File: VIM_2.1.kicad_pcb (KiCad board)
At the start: 2 copper layers, 83.9 x 89.5 mm, 160 parts, among them J1 BARREL_JACK, J2 Sliding switch, J3 Conn_01x05, J5 uart, J7 Conn_01x02, J8 Conn_01x03, P1 USB_OTG, P10 speed input, P12 CONN_02X03, P5 charging, P6 CONN_01X05, P9 throtle, Q1 Q_NPN_BEC, Q10 Q_NPN_BEC, Q11 Q_NPN_BEC, Q12 Q_NPN_BEC, Q13 Q_NPN_BEC, Q2 Q_NPN_BEC, Q3 Q_NPN_BEC, Q4 Q_NPN_BEC, Q5 Q_NPN_BEC, Q6 Q_NPN_BEC, Q7 Q_NPN_BEC, Q8 Q_NPN_BEC, Q9 Q_NPN_BEC, U1 STM32F405RG, U10 emmc, U11 TJA1042T/3, U12 NUP5150, U14 LD1117, U15 ufl, U16 ufl, U17 ufl, U18 ufl, U19 ublox_m8u, U2 MPU6050, U3 MIC29302, U4 ncs20062, U5 J502, U6 AP131-33, U7 MC6O, U8 lm2596 - 5v, U9 LD1117S33CTR, Y1 Crystal

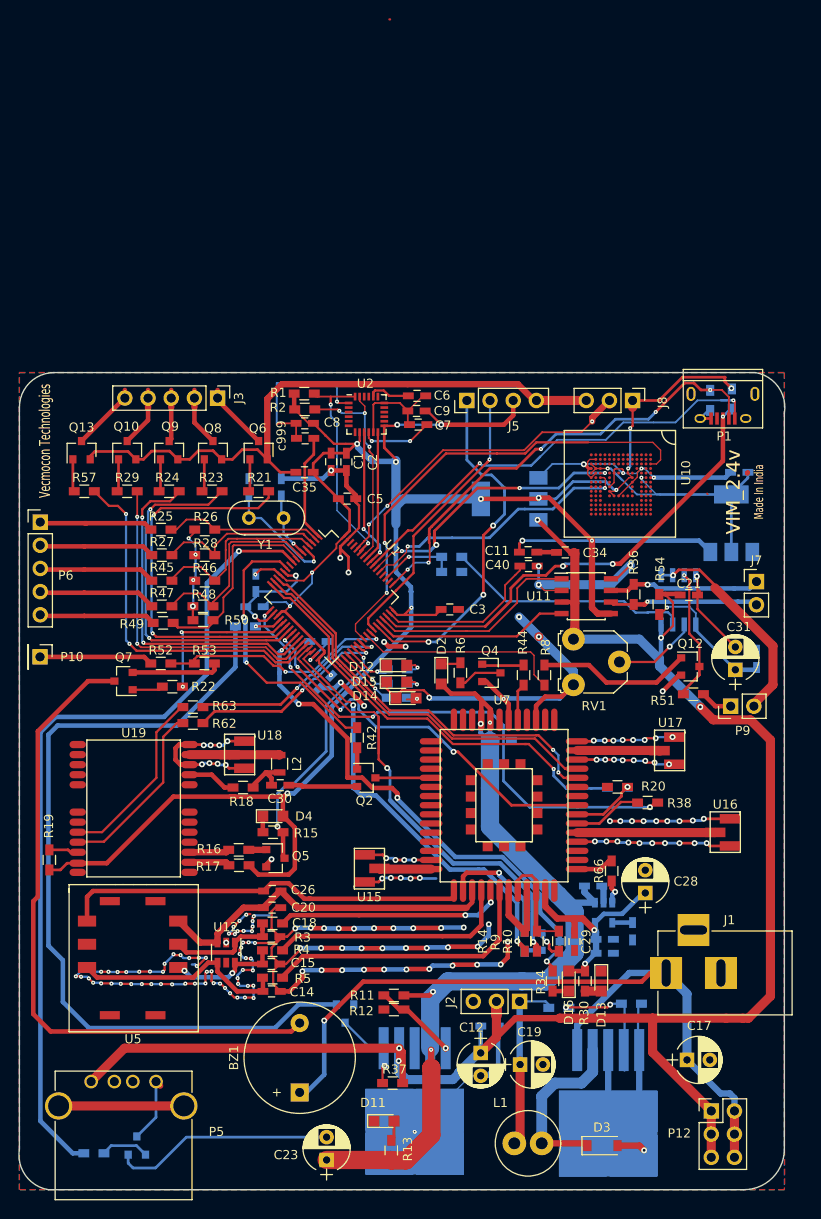
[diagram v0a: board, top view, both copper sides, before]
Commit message: Final pcb given to pcbpower
fleet management vim with following features
- ublox m8u, mc60
- mpu6050
- vibration sensor
- buzzer, switches, thottle bypass,
- sim interface according to quectel
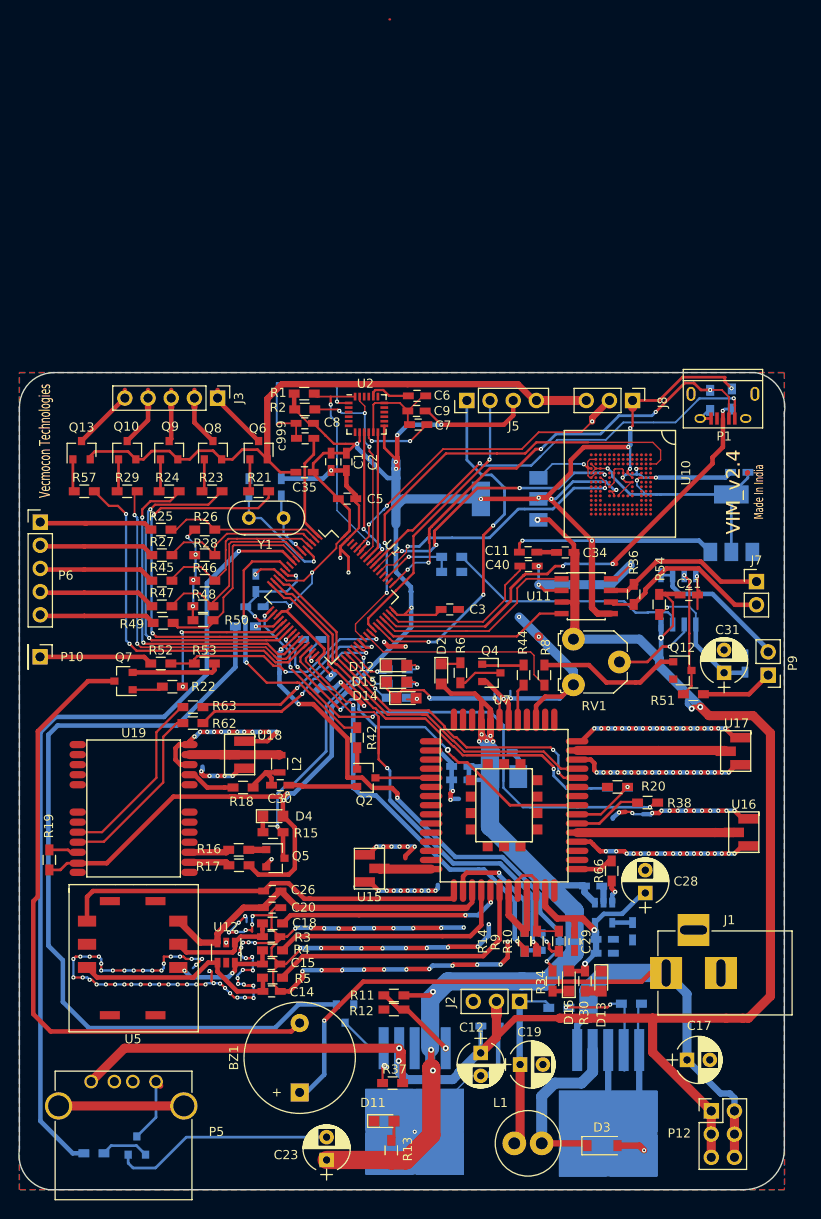
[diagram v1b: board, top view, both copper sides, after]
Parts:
- added C33: 100uF, Capacitors_Tantalum_SMD:CP_Tantalum_Case-B_EIA-3528-21_Reflow, B.Cu at (163.6, 105.9)
- added C36: 10pF, Capacitors_SMD:C_0603_HandSoldering, B.Cu at (158.8, 104.7)
- added C37: 33pF, Capacitors_SMD:C_0603_HandSoldering, B.Cu at (158.8, 106.2)
- C14, C15, C18, C20: value 10pF -> 33pF
- C23: value 100uF -> 470uF
- U10: footprint emmc1:eMMC1 -> emmc1:eMMC2.4
- U12: value NUP5150 -> CM1224
- U19: value ublox_m8u -> vim
- moved U17 7.24 mm to (189.5, 101.6)
- moved P9 5.33 mm to (192.5, 94.7), turned to 180 degrees
- moved U16 2.03 mm to (190.4, 110.5)
- moved C24 1.37 mm to (163.5, 103.2)
- moved C32 1.37 mm to (190.0, 93.5)
- moved C31 1.28 mm to (187.7, 94.5)
- moved Q12 0.97 mm to (183.1, 94.2)
- moved C10 0.71 mm to (142.6, 90.8)
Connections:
- J2 pad 3: (no net) -> Net-(J2-Pad3)
- P1 pad 4: (no net) -> Net-(P1-Pad4)
- P5 pad 2: (no net) -> Net-(P5-Pad2)
- P5 pad 3: (no net) -> Net-(P5-Pad3)
- U1 pad 10: (no net) -> Net-(U1-Pad10)
- U1 pad 50: (no net) -> Net-(U1-Pad50)
- U1 pad 52: (no net) -> Net-(U1-Pad52)
- U1 pad 61: (no net) -> Net-(U1-Pad61)
- U1 pad 62: (no net) -> Net-(U1-Pad62)
- U10 pad 10: (no net) -> Net-(U10-Pad10)
- U10 pad 100: (no net) -> Net-(U10-Pad100)
- U10 pad 101: (no net) -> Net-(U10-Pad101)
- U10 pad 102: (no net) -> Net-(U10-Pad102)
- U10 pad 103: (no net) -> Net-(U10-Pad103)
- U10 pad 104: (no net) -> Net-(U10-Pad104)
- U10 pad 106: (no net) -> Net-(U10-Pad106)
- U10 pad 107: (no net) -> Net-(U10-Pad107)
- U10 pad 108: (no net) -> Net-(U10-Pad108)
- U10 pad 109: (no net) -> Net-(U10-Pad109)
- U10 pad 11: (no net) -> Net-(U10-Pad11)
- U10 pad 110: (no net) -> Net-(U10-Pad110)
- U10 pad 111: (no net) -> Net-(U10-Pad111)
- U10 pad 112: (no net) -> Net-(U10-Pad112)
- U10 pad 113: (no net) -> Net-(U10-Pad113)
- U10 pad 114: (no net) -> Net-(U10-Pad114)
- U10 pad 115: (no net) -> Net-(U10-Pad115)
- U10 pad 116: (no net) -> Net-(U10-Pad116)
- U10 pad 117: (no net) -> Net-(U10-Pad117)
- U10 pad 118: (no net) -> Net-(U10-Pad118)
- U10 pad 119: (no net) -> Net-(U10-Pad119)
- U10 pad 12: (no net) -> Net-(U10-Pad12)
- U10 pad 120: (no net) -> Net-(U10-Pad120)
- U10 pad 121: (no net) -> Net-(U10-Pad121)
- U10 pad 122: (no net) -> Net-(U10-Pad122)
- U10 pad 123: (no net) -> Net-(U10-Pad123)
- U10 pad 124: (no net) -> Net-(U10-Pad124)
- U10 pad 125: (no net) -> Net-(U10-Pad125)
- U10 pad 126: (no net) -> Net-(U10-Pad126)
- U10 pad 127: (no net) -> Net-(U10-Pad127)
- U10 pad 128: (no net) -> Net-(U10-Pad128)
- U10 pad 129: (no net) -> Net-(U10-Pad129)
- U10 pad 13: (no net) -> Net-(U10-Pad13)
- U10 pad 130: (no net) -> Net-(U10-Pad130)
- U10 pad 131: (no net) -> Net-(U10-Pad131)
- U10 pad 132: (no net) -> Net-(U10-Pad132)
- U10 pad 133: (no net) -> Net-(U10-Pad133)
- U10 pad 134: (no net) -> Net-(U10-Pad134)
- U10 pad 135: (no net) -> Net-(U10-Pad135)
- U10 pad 136: (no net) -> Net-(U10-Pad136)
- U10 pad 137: (no net) -> Net-(U10-Pad137)
- U10 pad 138: (no net) -> Net-(U10-Pad138)
- U10 pad 139: (no net) -> Net-(U10-Pad139)
- U10 pad 14: (no net) -> Net-(U10-Pad14)
- U10 pad 140: (no net) -> Net-(U10-Pad140)
- U10 pad 141: (no net) -> Net-(U10-Pad141)
- U10 pad 142: (no net) -> Net-(U10-Pad142)
- U10 pad 143: (no net) -> Net-(U10-Pad143)
- U10 pad 144: (no net) -> Net-(U10-Pad144)
- U10 pad 145: (no net) -> Net-(U10-Pad145)
- U10 pad 146: (no net) -> Net-(U10-Pad146)
- U10 pad 147: (no net) -> Net-(U10-Pad147)
- U10 pad 148: (no net) -> Net-(U10-Pad148)
- U10 pad 149: (no net) -> Net-(U10-Pad149)
- U10 pad 15: (no net) -> Net-(U10-Pad15)
- U10 pad 150: (no net) -> Net-(U10-Pad150)
- U10 pad 151: (no net) -> Net-(U10-Pad151)
- U10 pad 152: (no net) -> Net-(U10-Pad152)
- U10 pad 153: (no net) -> Net-(U10-Pad153)
- U10 pad 16: (no net) -> Net-(U10-Pad16)
- U10 pad 17: (no net) -> Net-(U10-Pad17)
- U10 pad 18: (no net) -> Net-(U10-Pad18)
- U10 pad 19: (no net) -> Net-(U10-Pad19)
- U10 pad 2: (no net) -> Net-(U10-Pad2)
- U10 pad 20: (no net) -> Net-(U10-Pad20)
- U10 pad 3: (no net) -> Net-(U10-Pad3)
- U10 pad 4: (no net) -> Net-(U10-Pad4)
- U10 pad 41: (no net) -> Net-(U10-Pad41)
- U10 pad 42: (no net) -> Net-(U10-Pad42)
- U10 pad 43: (no net) -> Net-(U10-Pad43)
- U10 pad 44: (no net) -> Net-(U10-Pad44)
- U10 pad 45: (no net) -> Net-(U10-Pad45)
- U10 pad 46: (no net) -> Net-(U10-Pad46)
- U10 pad 47: (no net) -> Net-(U10-Pad47)
- U10 pad 48: (no net) -> Net-(U10-Pad48)
- U10 pad 5: (no net) -> Net-(U10-Pad5)
- U10 pad 51: (no net) -> Net-(U10-Pad51)
- U10 pad 52: (no net) -> Net-(U10-Pad52)
- U10 pad 53: (no net) -> Net-(U10-Pad53)
- U10 pad 54: (no net) -> Net-(U10-Pad54)
- U10 pad 55: (no net) -> Net-(U10-Pad55)
- U10 pad 56: (no net) -> Net-(U10-Pad56)
- U10 pad 57: (no net) -> Net-(U10-Pad57)
- U10 pad 58: (no net) -> Net-(U10-Pad58)
- U10 pad 59: (no net) -> Net-(U10-Pad59)
- U10 pad 6: (no net) -> Net-(U10-Pad6)
- U10 pad 60: (no net) -> Net-(U10-Pad60)
- U10 pad 61: (no net) -> Net-(U10-Pad61)
- U10 pad 62: (no net) -> Net-(U10-Pad62)
- U10 pad 63: (no net) -> Net-(U10-Pad63)
- U10 pad 64: (no net) -> Net-(U10-Pad64)
- U10 pad 65: (no net) -> Net-(U10-Pad65)
- U10 pad 66: (no net) -> Net-(U10-Pad66)
- U10 pad 67: (no net) -> Net-(U10-Pad67)
- U10 pad 68: (no net) -> Net-(U10-Pad68)
- U10 pad 69: (no net) -> Net-(U10-Pad69)
- U10 pad 7: (no net) -> Net-(U10-Pad7)
- U10 pad 70: (no net) -> Net-(U10-Pad70)
- U10 pad 71: (no net) -> Net-(U10-Pad71)
- U10 pad 72: (no net) -> Net-(U10-Pad72)
- U10 pad 73: (no net) -> Net-(U10-Pad73)
- U10 pad 74: (no net) -> Net-(U10-Pad74)
- U10 pad 75: (no net) -> Net-(U10-Pad75)
- U10 pad 76: (no net) -> Net-(U10-Pad76)
- U10 pad 78: (no net) -> Net-(U10-Pad78)
- U10 pad 79: (no net) -> Net-(U10-Pad79)
- U10 pad 8: (no net) -> Net-(U10-Pad8)
- U10 pad 80: (no net) -> Net-(U10-Pad80)
- U10 pad 81: (no net) -> Net-(U10-Pad81)
- U10 pad 82: (no net) -> Net-(U10-Pad82)
- U10 pad 83: (no net) -> Net-(U10-Pad83)
- U10 pad 84: (no net) -> Net-(U10-Pad84)
- U10 pad 85: (no net) -> Net-(U10-Pad85)
- U10 pad 86: (no net) -> Net-(U10-Pad86)
- U10 pad 87: (no net) -> Net-(U10-Pad87)
- U10 pad 88: (no net) -> Net-(U10-Pad88)
- U10 pad 89: (no net) -> Net-(U10-Pad89)
- U10 pad 9: (no net) -> Net-(U10-Pad9)
- U10 pad 90: (no net) -> Net-(U10-Pad90)
- U10 pad 91: (no net) -> Net-(U10-Pad91)
- U10 pad 92: (no net) -> Net-(U10-Pad92)
- U10 pad 93: (no net) -> Net-(U10-Pad93)
- U10 pad 94: (no net) -> Net-(U10-Pad94)
- U10 pad 95: (no net) -> Net-(U10-Pad95)
- U10 pad 96: (no net) -> Net-(U10-Pad96)
- U10 pad 97: (no net) -> Net-(U10-Pad97)
- U10 pad 98: (no net) -> Net-(U10-Pad98)
- U10 pad 99: (no net) -> Net-(U10-Pad99)
- U12 pad 5: (no net) -> Net-(U12-Pad5)
- U19 pad 1: (no net) -> Net-(U19-Pad1)
- U19 pad 14: (no net) -> Net-(U19-Pad14)
- U19 pad 15: (no net) -> Net-(U19-Pad15)
- U19 pad 16: (no net) -> Net-(U19-Pad16)
- U19 pad 17: (no net) -> Net-(U19-Pad17)
- U19 pad 18: (no net) -> Net-(U19-Pad18)
- U19 pad 19: (no net) -> Net-(U19-Pad19)
- U19 pad 4: (no net) -> Net-(U19-Pad4)
- U19 pad 5: (no net) -> Net-(U19-Pad5)
- U19 pad 6: (no net) -> Net-(U19-Pad6)
- U19 pad 7: (no net) -> Net-(U19-Pad7)
- U19 pad 8: (no net) -> Net-(U19-Pad8)
- U2 pad 14: (no net) -> Net-(U2-Pad14)
- U2 pad 15: (no net) -> Net-(U2-Pad15)
- U2 pad 16: (no net) -> Net-(U2-Pad16)
- U2 pad 17: (no net) -> Net-(U2-Pad17)
- U2 pad 19: (no net) -> Net-(U2-Pad19)
- U2 pad 2: (no net) -> Net-(U2-Pad2)
- U2 pad 21: (no net) -> Net-(U2-Pad21)
- U2 pad 22: (no net) -> Net-(U2-Pad22)
- U2 pad 3: (no net) -> Net-(U2-Pad3)
- U2 pad 4: (no net) -> Net-(U2-Pad4)
- U2 pad 5: (no net) -> Net-(U2-Pad5)
- U2 pad 6: (no net) -> Net-(U2-Pad6)
- U2 pad 7: (no net) -> Net-(U2-Pad7)
- U5 pad 2: (no net) -> Net-(U5-Pad2)
- U7 pad 1: (no net) -> Net-(U7-Pad1)
- U7 pad 10: (no net) -> Net-(U7-Pad10)
- U7 pad 11: (no net) -> Net-(U7-Pad11)
- U7 pad 12: (no net) -> Net-(U7-Pad12)
- U7 pad 13: (no net) -> Net-(U7-Pad13)
- U7 pad 2: (no net) -> Net-(U7-Pad2)
- U7 pad 29: (no net) -> Net-(U7-Pad29)
- U7 pad 3: (no net) -> Net-(U7-Pad3)
- U7 pad 30: (no net) -> Net-(U7-Pad30)
- U7 pad 36: (no net) -> Net-(U7-Pad36)
- U7 pad 37: (no net) -> Net-(U7-Pad37)
- U7 pad 4: (no net) -> Net-(U7-Pad4)
- U7 pad 43: (no net) -> /MC60/VDD_EXT
- U7 pad 46: (no net) -> Net-(U7-Pad46)
- U7 pad 52: (no net) -> Net-(U7-Pad52)
- U7 pad 53: (no net) -> Net-(U7-Pad53)
- U7 pad 54: (no net) -> Net-(U7-Pad54)
- U7 pad 55: (no net) -> Net-(U7-Pad55)
- U7 pad 56: (no net) -> Net-(U7-Pad56)
- U7 pad 57: (no net) -> Net-(U7-Pad57)
- U7 pad 58: (no net) -> Net-(U7-Pad58)
- U7 pad 59: (no net) -> Net-(U7-Pad59)
- U7 pad 6: (no net) -> Net-(U7-Pad6)
- U7 pad 60: (no net) -> Net-(U7-Pad60)
- U7 pad 61: (no net) -> Net-(U7-Pad61)
- U7 pad 62: (no net) -> Net-(U7-Pad62)
- U7 pad 63: (no net) -> Net-(U7-Pad63)
- U7 pad 64: (no net) -> Net-(U7-Pad64)
- U7 pad 65: (no net) -> Net-(U7-Pad65)
- U7 pad 66: (no net) -> Net-(U7-Pad66)
- U7 pad 67: (no net) -> Net-(U7-Pad67)
- U7 pad 68: (no net) -> Net-(U7-Pad68)
- U7 pad 7: (no net) -> Net-(U7-Pad7)
- U7 pad 8: (no net) -> Net-(U7-Pad8)
- U7 pad 9: (no net) -> Net-(U7-Pad9)
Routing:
- net GND: track 596.4 -> 646.7 mm, vias 164 -> 229
- net /MC60/vbat: track 127.8 -> 149.7 mm, vias 4 -> 8
- net +3V3: track 284.1 -> 299.4 mm, vias 18 -> 22
- net (no net): track 12.7 -> 2.79 mm, vias 13 -> 2
- net Net-(P9-Pad2): track 23.6 -> 16.1 mm, vias 1 -> 0
- net Net-(U17-Pad1): track 9.08 -> 16.3 mm
- net Net-(P9-Pad1): track 3.75 -> 7.96 mm
- net Net-(J7-Pad2): track 17.2 -> 20.9 mm, vias 1 -> 0
- net +5V: track 209.2 -> 212.2 mm, vias 5 -> 6
- net Net-(P1-Pad3): track 60.8 -> 58.2 mm
- net Net-(U16-Pad1): track 15.2 -> 17.2 mm
- net +12V: track 88.0 -> 89.6 mm
- net Net-(J7-Pad1): track 17.0 -> 18.5 mm, vias 1 -> 0
- net /ublox/gnss_rx: track 23.7 -> 22.5 mm
- net Net-(Q12-Pad1): track 17.0 -> 15.8 mm
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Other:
- net class Default: clearance 0.1 -> 0.125; via_dia 0.65 -> 0.46; via_drill 0.3 -> 0.17
- net class vbat added: clearance 0.125, trace_width 0.25, via_dia 0.65, via_drill 0.17
- net class vim: clearance 0.1 -> 0.125; via_drill 0.3 -> 0.35
- net class vim2 added: clearance 0.125, trace_width 0.25, via_dia 0.46, via_drill 0.2
- rule trace_clearance: 0.1 -> 0.125
- rule trace_min: 0.15 -> 0.125
- rule via_min_drill: 0.15 -> 0.17
- rule via_min_size: 0.45 -> 0.46
- board text added: "VIM_v2.4"
- board text removed: "VIM_2.4v"

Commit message: pcb print 28 jul
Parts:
- removed P10: speed input, Pin_Headers:Pin_Header_Straight_1x01_Pitch2.54mm
- removed P5: charging, Connectors:USB_A
- removed P6: CONN_01X05, Pin_Headers:Pin_Header_Straight_1x05_Pitch2.54mm
- removed U16: ufl, ufl:ufl_shield
- added AE1: Antenna, chip antenna:chip antenaa, F.Cu at (189.2, 112.0)
- added C41: 100nf, Capacitors_SMD:C_0603_HandSoldering, F.Cu at (149.9, 92.1)
- added D1: D, Diodes_SMD:D_SOD-123, B.Cu at (128.0, 138.2)
- added G***: LOGO, logo:logo3, F.Cu at (114.5, 140.4)
- added G***: LOGO, logo:logo5, B.Cu at (117.7, 141.4)
- added J4: Conn_01x06, Pin_Headers:Pin_Header_Straight_1x06_Pitch2.54mm, F.Cu at (114.6, 78.1)
- added P2: charging, Pin_Headers:Pin_Header_Straight_1x02_Pitch2.54mm, F.Cu at (141.9, 147.7)
- C12, C19: footprint Capacitors_THT:CP_Radial_D5.0mm_P2.50mm -> Capacitors_SMD:CP_Elec_6.3x5.7
- C17: footprint Capacitors_THT:CP_Radial_D5.0mm_P2.50mm -> Capacitors_SMD:CP_Elec_8x6.7
- C23: footprint Capacitors_THT:CP_Radial_D5.0mm_P2.50mm -> Capacitors_SMD:CP_Elec_8x10
- C28: footprint Capacitors_THT:CP_Radial_D5.0mm_P2.50mm -> Capacitors_SMD:CP_Elec_5x5.3
- C33: footprint Capacitors_Tantalum_SMD:CP_Tantalum_Case-B_EIA-3528-21_Reflow -> Capacitors_Tantalum_SMD:CP_Tantalum_Case-D_EIA-7343-31_Reflow
- L1: footprint Inductors_THT:L_Radial_D7.0mm_P3.00mm -> Inductors_SMD:L_7.3x7.3_H3.5
- moved Q11 12.0 mm to (135.2, 147.9), turned to 0 degrees
- moved C12 11.9 mm to (149.3, 138.2), turned to 180 degrees
- moved R13 10.3 mm to (141.8, 142.6), turned to 180 degrees
- moved C23 9.85 mm to (153.9, 146.3), turned to 180 degrees
- moved BZ1 9.48 mm to (131.8, 141.5), turned to 180 degrees
- moved D11 9.11 mm to (141.7, 141.1), turned to 180 degrees
- moved C17 7.65 mm to (176.1, 138.2)
- moved R7 6.89 mm to (125.3, 149.0)
- moved R37 6.74 mm to (151.3, 132.7)
- moved C32 6.10 mm to (186.6, 88.4)
- moved C33 5.41 mm to (164.3, 100.5)
- moved P12 3.22 mm to (185.0, 139.6), turned to 90 degrees
- moved C22 2.49 mm to (186.9, 72.3)
- moved Q12 2.03 mm to (181.1, 94.2)
- moved C28 1.87 mm to (180.7, 117.7), turned to 0 degrees
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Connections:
- R52 pad 1: Net-(P10-Pad1) -> /STM32 mcu/hall
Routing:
- net +12V: track 89.6 -> 113.5 mm, vias 1 -> 4
- net GND: track 646.7 -> 625.0 mm, vias 229 -> 230
- net +5V: track 212.2 -> 195.7 mm
- net Net-(P5-Pad5): track 13.7 -> 0.00 mm
- net Net-(P10-Pad1): track 12.4 -> 0.00 mm
- net /STM32 mcu/hall: track 0.00 -> 12.0 mm
- net /MC60/vbat: track 149.7 -> 139.6 mm
- net Net-(BZ1-Pad2): track 72.2 -> 62.2 mm
- net Net-(C19-Pad1): track 21.0 -> 27.4 mm, vias 0 -> 2
- net Net-(Q1-Pad3): track 9.33 -> 15.6 mm
- net Net-(D3-Pad1): track 19.4 -> 25.5 mm, vias 0 -> 3
- net Net-(J3-Pad5): track 7.85 -> 13.5 mm
- net Net-(R64-Pad1): track 14.3 -> 19.4 mm
- net Net-(J3-Pad1): track 8.17 -> 13.3 mm
- net /STM32 mcu/charging: track 91.1 -> 94.9 mm
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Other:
- outline, holes or cut-outs redrawn

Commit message: bt
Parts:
- AE1: footprint chip antenna:chip antenaa -> ANTENNASMD:bluetooth_antenna
- moved AE1 0.33 mm to (188.8, 111.9)
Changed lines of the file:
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@@
   (general
     (links 397)
-    (no_connects 0)
-    (area 110.362445 61.519999 194.437555 151.205001)
+    (no_connects 67)
+    (area 109.932181 22.646319 206.605 157.560001)
     (thickness 1.6)
     (drawings 18)
@@
   )
   (setup
-    (last_trace_width 0.5)
+    (last_trace_width 0.25)
     (user_trace_width 0.125)
     (user_trace_width 0.2)
@@
     )
   )
-  (module "chip antenna:chip antenaa" (layer F.Cu)
-    (at 189.1538 111.9759)
-    (fp_text reference AE1 (at 1.0668 -1.778) (layer F.SilkS)
-      (effects (font (size 1 1) (thickness 0.15)))
-    )
-    (fp_text value Antenna (at 1.1684 1.4224) (layer F.Fab)
-      (effects (font (size 1 1) (thickness 0.15)))
-    )
-    (fp_arc (start 0.6604 0) (end 1.0668 -0.4064) (angle 90) (layer F.SilkS) (width 0.15))
-    (fp_line (start -0.762 -0.9144) (end 3.7084 -0.9144) (layer F.SilkS) (width 0.15))
-    (fp_line (start 3.7084 -0.9144) (end 3.7592 -0.9144) (layer F.SilkS) (width 0.15))
-    (fp_line (start 3.7592 -0.9144) (end 3.7592 0.9144) (layer F.SilkS) (width 0.15))
-    (fp_line (start 3.7592 0.9144) (end -0.8128 0.9144) (layer F.SilkS) (width 0.15))
-    (fp_line (start -0.8128 0.9144) (end -0.8128 -0.9144) (layer F.SilkS) (width 0.15))
-    (pad 1 smd rect (at 0 0) (size 1.5 1.8) (layers F.Cu F.Paste F.Mask)
-      (net 327 "Net-(AE1-Pad1)"))
-    (pad "" smd rect (at 3 0) (size 1.5 1.8) (layers F.Cu F.Paste F.Mask))
-  )
   (module Capacitors_Tantalum_SMD:CP_Tantalum_Case-D_EIA-7343-31_Reflow (layer B.Cu)
     (at 164.2618 100.4951)
@@
       (xy -4.097867 0.143934)) (layer B.SilkS) (width 0.01))
   )
+  (module ANTENNASMD:bluetooth_antenna (layer F.Cu)
+    (at 188.8236 111.9251)
+    (fp_text reference AE1 (at 3.175 2.54) (layer F.SilkS)
+      (effects (font (size 1 1) (thickness 0.15)))
+    )
+    (fp_text value Antenna (at 2.54 -2.54) (layer F.Fab)
+      (effects (font (size 1 1) (thickness 0.15)))
+    )
+    (pad 1 smd rect (at 0 0) (size 0.8 2) (layers F.Cu F.Paste F.Mask)
+      (net 327 "Net-(AE1-Pad1)"))
+    (pad "" smd rect (at 4.7 0) (size 0.8 2) (layers F.Cu F.Paste F.Mask))
+    (pad "" smd rect (at 2.35 -0.85) (size 2.8 0.7) (layers F.Cu F.Paste F.Mask))
+    (pad "" smd rect (at 2.35 0.85) (size 2.8 0.7) (layers F.Cu F.Paste F.Mask))
+  )
   (gr_circle (center 114.1222 65.0367) (end 116.0272 65.0367) (layer Edge.Cuts) (width 0.15))
   (gr_circle (center 191.1858 70.9803) (end 193.0908 70.9803) (layer Edge.Cuts) (width 0.15))
@@
   (segment (start 117.2718 92.75) (end 124.162 92.75) (width 0.5) (layer F.Cu) (net 333))
   (segment (start 124.162 92.75) (end 124.884 93.472) (width 0.5) (layer F.Cu) (net 333))
-  (zone (net 2) (net_name GND) (layer B.Cu) (hatch edge 0.508)
+  (zone (net 0) (net_name "") (layer B.Cu) (hatch edge 0.508)
     (connect_pads (clearance 0.508))
     (min_thickness 0.254)
-    (fill yes (arc_segments 16) (thermal_gap 0.508) (thermal_bridge_width 0.508))
+    (keepout (tracks allowed) (vias allowed) (copperpour not_allowed))
+    (fill (arc_segments 16) (thermal_gap 0.508) (thermal_bridge_width 0.508))
     (polygon
       (pts
-        (xy 194.31 151.13) (xy 110.49 151.13) (xy 110.49 61.595) (xy 194.31 61.595)
+        (xy 194.5132 118.6053) (xy 188.1632 118.6053) (xy 188.1632 105.9053) (xy 194.5132 105.9053)
       )
     )
   )
-  (zone (net 2) (net_name GND) (layer F.Cu) (hatch edge 0.508)
-    (connect_pads (clearance 0.16))
+  (zone (net 0) (net_name "") (layer F.Cu) (hatch edge 0.508)
+    (connect_pads (clearance 0.508))
     (min_thickness 0.254)
-    (fill yes (arc_segments 16) (thermal_gap 0.508) (thermal_bridge_width 0.508))
+    (keepout (tracks allowed) (vias allowed) (copperpour not_allowed))
+    (fill (arc_segments 16) (thermal_gap 0.508) (thermal_bridge_width 0.508))
     (polygon
       (pts
-        (xy 194.31 140.410252) (xy 194.34 150.906) (xy 194.31 150.906) (xy 194.31 151.13) (xy 110.49 151.13)
-        (xy 110.49 61.595) (xy 194.31 61.595)
+        (xy 194.5132 118.6053) (xy 188.1632 118.6053) (xy 188.1632 105.9053) (xy 194.5132 105.9053)
       )
     )
   )
-  (zone (net 0) (net_name "") (layer B.Cu) (hatch edge 0.508)
+  (zone (net 2) (net_name GND) (layer B.Cu) (hatch edge 0.508)
     (connect_pads (clearance 0.508))
     (min_thickness 0.254)
-    (keepout (tracks allowed) (vias allowed) (copperpour not_allowed))
     (fill (arc_segments 16) (thermal_gap 0.508) (thermal_bridge_width 0.508))
     (polygon
       (pts
-        (xy 194.5132 118.6053) (xy 188.1632 118.6053) (xy 188.1632 105.9053) (xy 194.5132 105.9053)
+        (xy 194.31 151.13) (xy 110.49 151.13) (xy 110.49 61.595) (xy 194.31 61.595)
       )
     )
   )
-  (zone (net 0) (net_name "") (layer F.Cu) (hatch edge 0.508)
-    (connect_pads (clearance 0.508))
+  (zone (net 2) (net_name GND) (layer F.Cu) (hatch edge 0.508)
+    (connect_pads (clearance 0.16))
     (min_thickness 0.254)
-    (keepout (tracks allowed) (vias allowed) (copperpour not_allowed))
     (fill (arc_segments 16) (thermal_gap 0.508) (thermal_bridge_width 0.508))
     (polygon
       (pts
-        (xy 194.5132 118.6053) (xy 188.1632 118.6053) (xy 188.1632 105.9053) (xy 194.5132 105.9053)
+        (xy 194.31 140.410252) (xy 194.34 150.906) (xy 194.31 150.906) (xy 194.31 151.13) (xy 110.49 151.13)
+        (xy 110.49 61.595) (xy 194.31 61.595)
       )
     )

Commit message: final
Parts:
- removed P12: CONN_02X03, Pin_Headers:Pin_Header_Straight_2x03_Pitch2.54mm
- removed P9: throtle, Pin_Headers:Pin_Header_Straight_1x02_Pitch2.54mm
- added J10: Conn_01x03, Pin_Headers:Pin_Header_Straight_1x03_Pitch2.54mm, F.Cu at (114.9, 91.8)
- added J6: Conn_01x03, Pin_Headers:Pin_Header_Straight_1x03_Pitch2.54mm, F.Cu at (185.7, 136.1)
- added J9: Conn_01x03, Pin_Headers:Pin_Header_Straight_1x03_Pitch2.54mm, F.Cu at (114.6, 78.1)
- J4: value Conn_01x06 -> Conn_01x03; footprint Pin_Headers:Pin_Header_Straight_1x06_Pitch2.54mm -> Pin_Headers:Pin_Header_Straight_1x03_Pitch2.54mm
- J7: value Conn_01x02 -> uart; footprint Pin_Headers:Pin_Header_Straight_1x02_Pitch2.54mm -> Pin_Headers:Pin_Header_Straight_1x04_Pitch2.54mm
- moved J4 95.7 mm to (185.5, 142.3), turned to 90 degrees
- moved Q12 4.09 mm to (179.9, 98.2)
- moved C31 3.97 mm to (181.9, 94.6)
- moved G*** 1.41 mm to (118.9, 142.1)
- moved J7 1.05 mm to (189.6, 85.7)
- moved R51 0.57 mm to (184.2, 97.4)
- moved G*** 0.24 mm to (114.6, 140.6)
- moved AE1 0.06 mm to (188.8, 111.9)
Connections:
- J4 pad 1: Net-(J4-Pad1) -> +5V
- J4 pad 2: Net-(J4-Pad2) -> +5V
- J4 pad 3: Net-(J4-Pad3) -> +5V
- R25 pad 1: Net-(J4-Pad1) -> Net-(J9-Pad1)
- R27 pad 1: Net-(J4-Pad2) -> Net-(J9-Pad2)
- R45 pad 1: Net-(J4-Pad3) -> Net-(J9-Pad3)
- R47 pad 1: Net-(J4-Pad4) -> Net-(J10-Pad1)
- R49 pad 1: Net-(J4-Pad5) -> Net-(J10-Pad2)
- R51 pad 2: Net-(P9-Pad1) -> /STM32 mcu/a
- U4 pad 1: Net-(P9-Pad2) -> /STM32 mcu/b
- U4 pad 2: Net-(P9-Pad2) -> /STM32 mcu/b
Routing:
- net Net-(J9-Pad3): track 0.00 -> 22.9 mm
- net Net-(J9-Pad2): track 0.00 -> 21.0 mm
- net Net-(P9-Pad2): track 14.8 -> 0.00 mm, vias 1 -> 0
- net /STM32 mcu/b: track 0.00 -> 13.0 mm, vias 0 -> 1
- net Net-(J10-Pad2): track 0.00 -> 12.5 mm
- net Net-(J4-Pad3): track 12.0 -> 0.00 mm
- net Net-(J10-Pad1): track 0.00 -> 12.0 mm
- net Net-(J4-Pad5): track 11.6 -> 0.00 mm
- net Net-(J4-Pad1): track 11.6 -> 0.00 mm
- net Net-(J4-Pad2): track 11.6 -> 0.00 mm
- net Net-(J4-Pad4): track 11.5 -> 0.00 mm
- net Net-(J9-Pad1): track 0.00 -> 10.7 mm
- net +12V: track 113.5 -> 120.5 mm
- net Net-(P9-Pad1): track 6.58 -> 0.00 mm
- net /STM32 mcu/a: track 0.00 -> 5.92 mm
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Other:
- outline, holes or cut-outs redrawn

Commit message: PCB SENT TO PCB POWER
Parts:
- removed the G*** at (118.9, 142.1)
- added G***: LOGO, logo:logo14, B.Cu at (120.3, 118.0)
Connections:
- U1 pad 10: Net-(U1-Pad10) -> /STM32 mcu/charging
- U1 pad 7: /STM32 mcu/in4 -> Net-(U1-Pad7)
- U1 pad 8: /STM32 mcu/in5 -> /STM32 mcu/in4
- U1 pad 9: /STM32 mcu/charging -> /STM32 mcu/in5
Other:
- board text added: "VECMOCON TECHNOLOGIES"
